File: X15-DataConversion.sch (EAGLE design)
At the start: 25 parts, among them Y1 ECS-80-18-4X

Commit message: layout mostly done
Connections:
- net 3.3V renamed 3V3
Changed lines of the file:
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@@
 <part name="R6" library="SparkFun-Resistors" deviceset="RESISTOR" device="0603" value="120"/>
 <part name="R7" library="SparkFun-Resistors" deviceset="RESISTOR" device="0603" value="120"/>
-<part name="GND10" library="supply1" library_urn="urn:adsk.eagle:library:371" deviceset="GND" device=""/>
 <part name="R9" library="SparkFun-Resistors" deviceset="RESISTOR" device="0603" value="0"/>
 <part name="C7" library="SparkFun-RF" deviceset="0.1UF" device="-0603-25V-5%" value="18pF"/>
@@
 <part name="R8" library="SparkFun-Resistors" deviceset="RESISTOR" device="0603" value="0"/>
 <part name="GND9" library="supply1" library_urn="urn:adsk.eagle:library:371" deviceset="GND" device=""/>
+<part name="GND10" library="supply1" library_urn="urn:adsk.eagle:library:371" deviceset="GND" device=""/>
 </parts>
 <sheets>
@@
 <attribute name="VALUE" x="111.76" y="46.736" size="1.778" layer="96" font="vector" align="top-center"/>
 </instance>
-<instance part="GND10" gate="1" x="101.6" y="66.04" smashed="yes" rot="R90">
-<attribute name="VALUE" x="104.14" y="63.5" size="1.778" layer="96" rot="R90"/>
-</instance>
 <instance part="R9" gate="G$1" x="147.32" y="40.64" smashed="yes" rot="R90">
 <attribute name="NAME" x="145.796" y="40.64" size="1.778" layer="95" font="vector" rot="R90" align="bottom-center"/>
@@
 <instance part="GND9" gate="1" x="99.06" y="40.64" smashed="yes">
 <attribute name="VALUE" x="96.52" y="38.1" size="1.778" layer="96"/>
+</instance>
+<instance part="GND10" gate="1" x="101.6" y="66.04" smashed="yes" rot="R90">
+<attribute name="VALUE" x="104.14" y="63.5" size="1.778" layer="96" rot="R90"/>
 </instance>
 </instances>
@@
 <wire x1="93.98" y1="165.1" x2="88.9" y2="165.1" width="0.1524" layer="91"/>
 <junction x="88.9" y="165.1"/>
-</segment>
-<segment>
-<pinref part="GND3" gate="1" pin="GND"/>
-<pinref part="STM" gate="G$1" pin="VSS_2"/>
-<wire x1="127" y1="93.98" x2="127" y2="99.06" width="0.1524" layer="91"/>
 </segment>
 <segment>
@@
 </segment>
 <segment>
-<pinref part="CAN_TRANCEIVER" gate="G$1" pin="RS"/>
-<pinref part="GND10" gate="1" pin="GND"/>
-<wire x1="93.98" y1="66.04" x2="99.06" y2="66.04" width="0.1524" layer="91"/>
-</segment>
-<segment>
 <pinref part="C7" gate="G$1" pin="2"/>
 <wire x1="137.16" y1="20.32" x2="137.16" y2="17.78" width="0.1524" layer="91"/>
@@
 <wire x1="99.06" y1="50.8" x2="99.06" y2="43.18" width="0.1524" layer="91"/>
 <pinref part="GND9" gate="1" pin="GND"/>
+</segment>
+<segment>
+<pinref part="GND3" gate="1" pin="GND"/>
+<pinref part="STM" gate="G$1" pin="VSS_2"/>
+<wire x1="127" y1="93.98" x2="127" y2="99.06" width="0.1524" layer="91"/>
+</segment>
+<segment>
+<pinref part="GND10" gate="1" pin="GND"/>
+<pinref part="CAN_TRANCEIVER" gate="G$1" pin="RS"/>
+<wire x1="99.06" y1="66.04" x2="93.98" y2="66.04" width="0.1524" layer="91"/>
 </segment>
 </net>
@@
 </segment>
 </net>
-<net name="3.3V" class="0">
+<net name="3V3" class="0">
 <segment>
 <pinref part="STM" gate="G$1" pin="VDDA"/>
@@
 <pinref part="STM" gate="G$1" pin="PF0-OSC_IN"/>
 <wire x1="78.74" y1="139.7" x2="68.58" y2="139.7" width="0.1524" layer="91"/>
+<label x="58.42" y="139.7" size="1.778" layer="95"/>
 </segment>
 <segment>
@@
 <pinref part="STM" gate="G$1" pin="PF1-OSC_OUT"/>
 <wire x1="78.74" y1="134.62" x2="68.58" y2="134.62" width="0.1524" layer="91"/>
-</segment>
-<segment>
+<label x="53.34" y="134.62" size="1.778" layer="95"/>
+</segment>
+<segment>

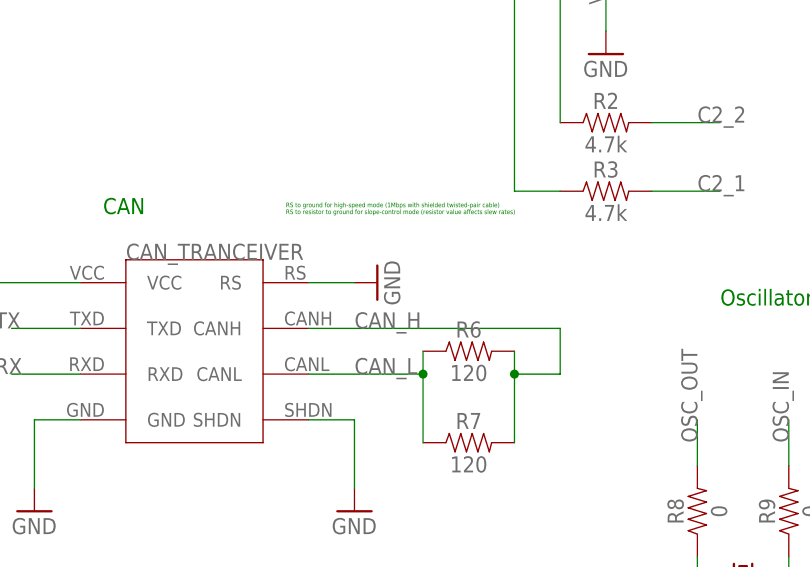
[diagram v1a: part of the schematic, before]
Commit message: fixing board layout
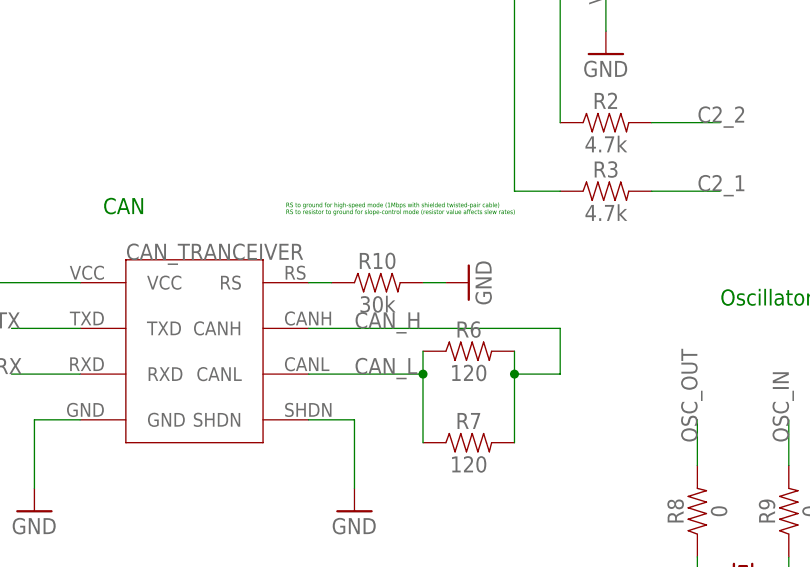
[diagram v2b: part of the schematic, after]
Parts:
- added R10: 30k, SparkFun-Resistors:RESISTOR0603
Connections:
- new net N$2: CAN_TRANCEIVER.RS, R10.1
- net GND: now also R10.2; no longer CAN_TRANCEIVER.RS
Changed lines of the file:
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@@
 <part name="GND9" library="supply1" library_urn="urn:adsk.eagle:library:371" deviceset="GND" device=""/>
 <part name="GND10" library="supply1" library_urn="urn:adsk.eagle:library:371" deviceset="GND" device=""/>
+<part name="R10" library="SparkFun-Resistors" deviceset="RESISTOR" device="0603" value="30k"/>
 </parts>
 <sheets>
@@
 <attribute name="VALUE" x="96.52" y="38.1" size="1.778" layer="96"/>
 </instance>
-<instance part="GND10" gate="1" x="101.6" y="66.04" smashed="yes" rot="R90">
-<attribute name="VALUE" x="104.14" y="63.5" size="1.778" layer="96" rot="R90"/>
+<instance part="GND10" gate="1" x="111.76" y="66.04" smashed="yes" rot="R90">
+<attribute name="VALUE" x="114.3" y="63.5" size="1.778" layer="96" rot="R90"/>
+</instance>
+<instance part="R10" gate="G$1" x="101.6" y="66.04" smashed="yes">
+<attribute name="NAME" x="101.6" y="67.564" size="1.778" layer="95" font="vector" align="bottom-center"/>
+<attribute name="VALUE" x="101.6" y="64.516" size="1.778" layer="96" font="vector" align="top-center"/>
 </instance>
 </instances>
@@
 </segment>
 <segment>
+<pinref part="R10" gate="G$1" pin="2"/>
 <pinref part="GND10" gate="1" pin="GND"/>
-<pinref part="CAN_TRANCEIVER" gate="G$1" pin="RS"/>
-<wire x1="99.06" y1="66.04" x2="93.98" y2="66.04" width="0.1524" layer="91"/>
+<wire x1="106.68" y1="66.04" x2="109.22" y2="66.04" width="0.1524" layer="91"/>
 </segment>
 </net>
@@
 </segment>
 </net>
+<net name="N$2" class="0">
+<segment>
+<pinref part="CAN_TRANCEIVER" gate="G$1" pin="RS"/>
+<pinref part="R10" gate="G$1" pin="1"/>
+<wire x1="93.98" y1="66.04" x2="96.52" y2="66.04" width="0.1524" layer="91"/>
+</segment>
+</net>

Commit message: cleaning up board layout
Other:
- note removed: "RS to ground for high-speed mode (1Mbps with shielded twisted-pair cable) RS to resistor to ground for slope-control mode (resistor value affects slew rates)"
- moved on the sheet: C6, CAN_TRANCEIVER, CONNECTOR1, D3, R10, R5, R6, R7, U$1

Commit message: alumni review changes
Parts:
- removed D1: Green, SparkFun-LED:LED-GREEN-0603-WE
- removed D3: Orange, SparkFun-LED:LED0603
- added LED1, LED2: LSM0805452VLED_05452V_VCC, X15-Data-Conversion-Parts:LSM0805452VLED_05452V_VCC
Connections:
- net GND: now also LED1.2, LED2.2; no longer D1.C, D3.C
- net N$1: now also LED1.1; no longer D3.A
- net N$11: now also LED2.1; no longer D1.A
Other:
- moved on the sheet: R6, R7

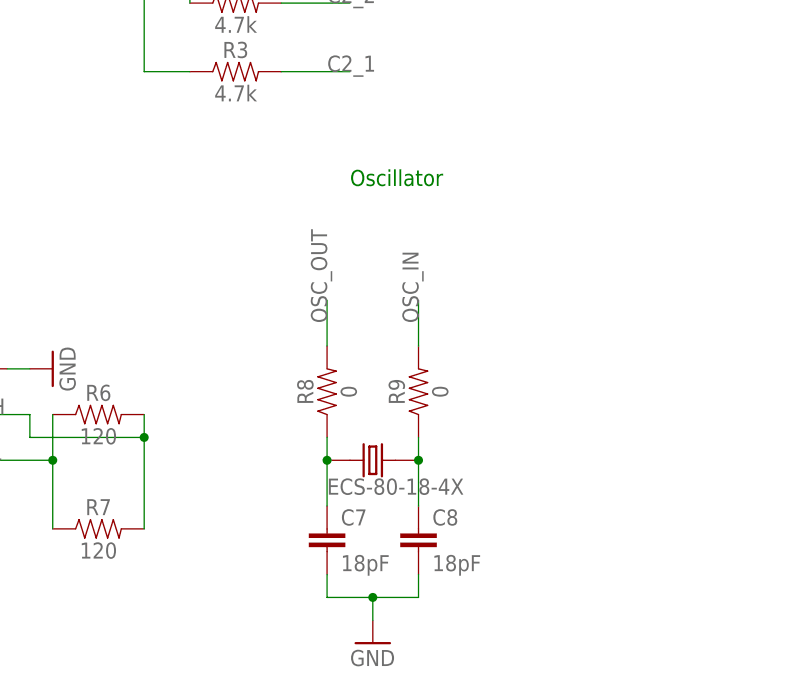
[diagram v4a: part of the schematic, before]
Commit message: removed oscillator and fixed trace widths
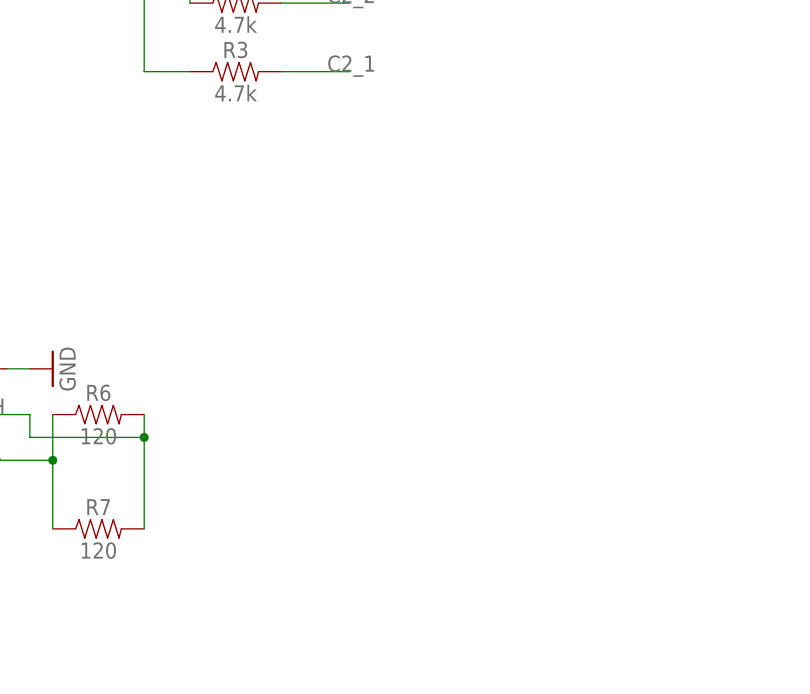
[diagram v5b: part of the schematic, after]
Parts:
- removed C7, C8: 18pF, SparkFun-RF:0.1UF-0603-25V-5%
- removed R8, R9: 0, SparkFun-Resistors:RESISTOR0603
- removed Y1: ECS-80-18-4X, X15-Data-Conversion-Parts:ECS-80-18-4X
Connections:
- removed net N$3: C7.1, R8.1, Y1.1
- removed net N$4: C8.1, R9.1, Y1.2
- net GND: no longer C7.2, C8.2
- net OSC_IN: no longer R9.2
- net OSC_OUT: no longer R8.2
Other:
- note removed: "Oscillator"
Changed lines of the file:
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@@
 <part name="GND7" library="supply1" library_urn="urn:adsk.eagle:library:371" deviceset="GND" device=""/>
 <part name="GND8" library="supply1" library_urn="urn:adsk.eagle:library:371" deviceset="GND" device=""/>
-<part name="R9" library="SparkFun-Resistors" deviceset="RESISTOR" device="0603" value="0"/>
-<part name="C7" library="SparkFun-RF" deviceset="0.1UF" device="-0603-25V-5%" value="18pF"/>
-<part name="C8" library="SparkFun-RF" deviceset="0.1UF" device="-0603-25V-5%" value="18pF"/>
-<part name="GND11" library="supply1" library_urn="urn:adsk.eagle:library:371" deviceset="GND" device=""/>
-<part name="Y1" library="X15-Data-Conversion-Parts" deviceset="ECS-80-18-4X" device="" package3d_urn="urn:adsk.eagle:package:38192067/2"/>
-<part name="R8" library="SparkFun-Resistors" deviceset="RESISTOR" device="0603" value="0"/>
 <part name="GND9" library="supply1" library_urn="urn:adsk.eagle:library:371" deviceset="GND" device=""/>
 <part name="GND10" library="supply1" library_urn="urn:adsk.eagle:library:371" deviceset="GND" device=""/>
@@
 <text x="205.74" y="81.28" size="1.778" layer="91">Connectors</text>
 <text x="66.04" y="50.8" size="1.778" layer="91">CAN</text>
-<text x="139.7" y="63.5" size="1.778" layer="91">Oscillator</text>
 <text x="190.5" y="152.4" size="1.778" layer="91">Pin 1 (VDD)</text>
 <text x="210.82" y="152.4" size="1.778" layer="91">Pin 17 (VDDIO2)</text>
@@
 <instance part="GND8" gate="1" x="58.42" y="17.78" smashed="yes">
 <attribute name="VALUE" x="55.88" y="15.24" size="1.778" layer="96"/>
-</instance>
-<instance part="R9" gate="G$1" x="147.32" y="40.64" smashed="yes" rot="R90">
-<attribute name="NAME" x="145.796" y="40.64" size="1.778" layer="95" font="vector" rot="R90" align="bottom-center"/>
-<attribute name="VALUE" x="148.844" y="40.64" size="1.778" layer="96" font="vector" rot="R90" align="top-center"/>
-</instance>
-<instance part="C7" gate="G$1" x="137.16" y="22.86" smashed="yes">
-<attribute name="NAME" x="138.684" y="25.781" size="1.778" layer="95" font="vector"/>
-<attribute name="VALUE" x="138.684" y="20.701" size="1.778" layer="96" font="vector"/>
-</instance>
-<instance part="C8" gate="G$1" x="147.32" y="22.86" smashed="yes">
-<attribute name="NAME" x="148.844" y="25.781" size="1.778" layer="95" font="vector"/>
-<attribute name="VALUE" x="148.844" y="20.701" size="1.778" layer="96" font="vector"/>
-</instance>
-<instance part="GND11" gate="1" x="142.24" y="12.7" smashed="yes">
-<attribute name="VALUE" x="139.7" y="10.16" size="1.778" layer="96"/>
-</instance>
-<instance part="Y1" gate="G$1" x="142.24" y="33.02" smashed="yes">
-<attribute name="VALUE" x="137.14506875" y="29.19645" size="1.78431875" layer="96"/>
-</instance>
-<instance part="R8" gate="G$1" x="137.16" y="40.64" smashed="yes" rot="R90">
-<attribute name="NAME" x="135.636" y="40.64" size="1.778" layer="95" font="vector" rot="R90" align="bottom-center"/>
-<attribute name="VALUE" x="138.684" y="40.64" size="1.778" layer="96" font="vector" rot="R90" align="top-center"/>
 </instance>
 <instance part="GND9" gate="1" x="93.98" y="17.78" smashed="yes">
@@
 </segment>
 <segment>
-<pinref part="C7" gate="G$1" pin="2"/>
-<wire x1="137.16" y1="20.32" x2="137.16" y2="17.78" width="0.1524" layer="91"/>
-<wire x1="137.16" y1="17.78" x2="142.24" y2="17.78" width="0.1524" layer="91"/>
-<pinref part="C8" gate="G$1" pin="2"/>
-<wire x1="142.24" y1="17.78" x2="147.32" y2="17.78" width="0.1524" layer="91"/>
-<wire x1="147.32" y1="17.78" x2="147.32" y2="20.32" width="0.1524" layer="91"/>
-<wire x1="142.24" y1="17.78" x2="142.24" y2="15.24" width="0.1524" layer="91"/>
-<junction x="142.24" y="17.78"/>
-<pinref part="GND11" gate="1" pin="GND"/>
-</segment>
-<segment>
 <pinref part="CAN_TRANCEIVER" gate="G$1" pin="SHDN"/>
 <wire x1="88.9" y1="27.94" x2="93.98" y2="27.94" width="0.1524" layer="91"/>
@@
 <label x="58.42" y="139.7" size="1.778" layer="95"/>
 </segment>
-<segment>
-<pinref part="R9" gate="G$1" pin="2"/>
-<wire x1="147.32" y1="45.72" x2="147.32" y2="50.8" width="0.1524" layer="91"/>
-<label x="147.32" y="48.26" size="1.778" layer="95" rot="R90"/>
-</segment>
 </net>
 <net name="OSC_OUT" class="0">
@@
 <label x="53.34" y="134.62" size="1.778" layer="95"/>
 </segment>
-<segment>
-<pinref part="R8" gate="G$1" pin="2"/>
-<wire x1="137.16" y1="45.72" x2="137.16" y2="50.8" width="0.1524" layer="91"/>
-<label x="137.16" y="48.26" size="1.778" layer="95" rot="R90"/>
-</segment>
-</net>
-<net name="N$3" class="0">
-<segment>
-<pinref part="Y1" gate="G$1" pin="1"/>
-<pinref part="R8" gate="G$1" pin="1"/>
-<wire x1="137.16" y1="33.02" x2="137.16" y2="35.56" width="0.1524" layer="91"/>
-<pinref part="C7" gate="G$1" pin="1"/>
-<wire x1="137.16" y1="27.94" x2="137.16" y2="33.02" width="0.1524" layer="91"/>
-<junction x="137.16" y="33.02"/>
-</segment>
-</net>
-<net name="N$4" class="0">
-<segment>
-<pinref part="Y1" gate="G$1" pin="2"/>
-<pinref part="R9" gate="G$1" pin="1"/>
-<wire x1="147.32" y1="33.02" x2="147.32" y2="35.56" width="0.1524" layer="91"/>
-<pinref part="C8" gate="G$1" pin="1"/>
-<wire x1="147.32" y1="27.94" x2="147.32" y2="33.02" width="0.1524" layer="91"/>
-<junction x="147.32" y="33.02"/>
-</segment>
-</net>
+</net>

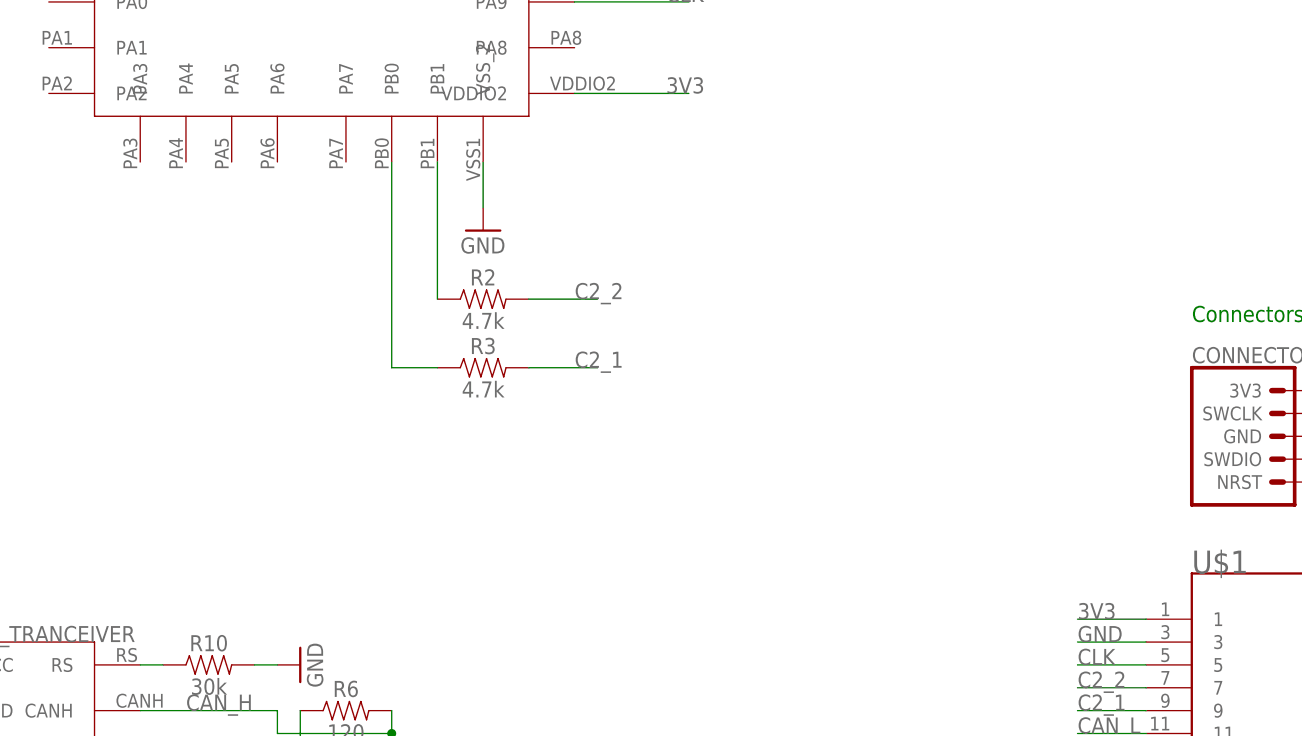
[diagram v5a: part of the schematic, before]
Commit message: added 5 pin connector
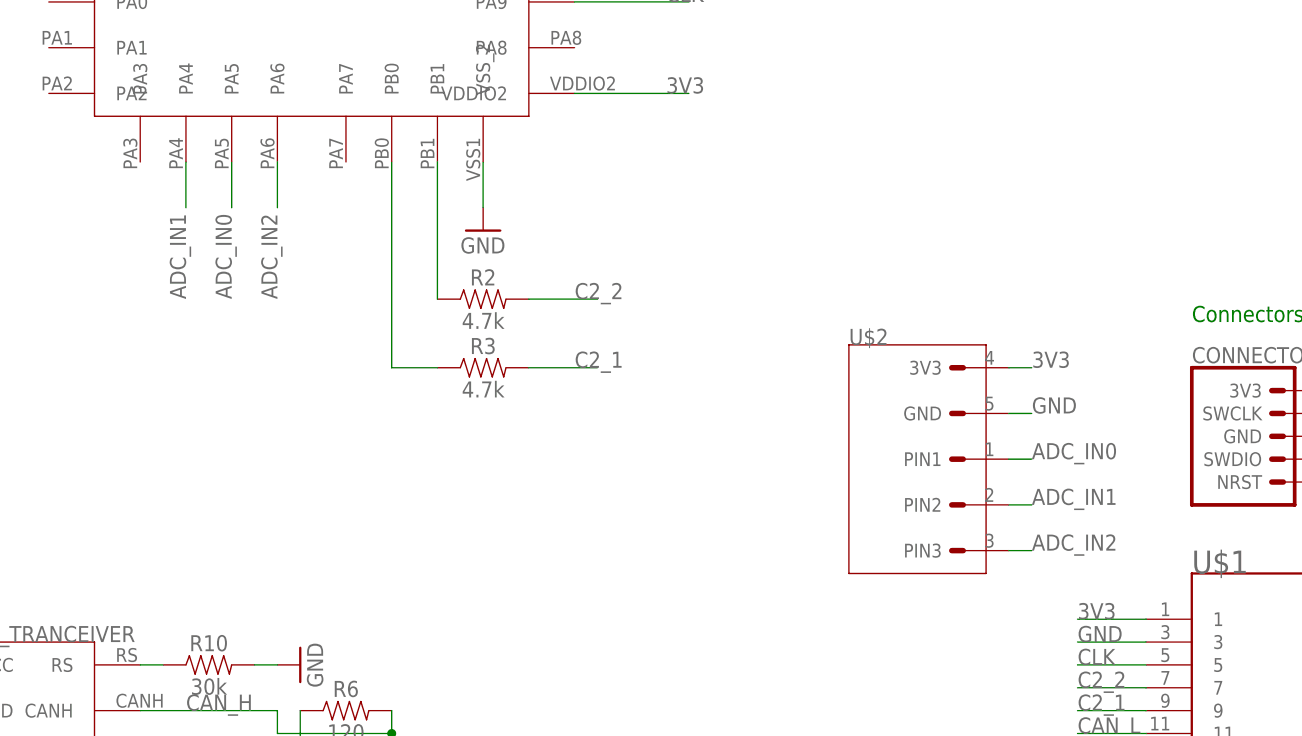
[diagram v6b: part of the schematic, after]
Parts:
- added U$2: STM_CONN, X15-Data-Conversion-Parts:STM_CONN
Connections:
- new net ADC_IN0: STM.PA5, U$2.PIN1
- new net ADC_IN1: STM.PA4, U$2.PIN2
- new net ADC_IN2: STM.PA6, U$2.PIN3
- net 3V3: now also U$2.3V3
- net GND: now also U$2.GND
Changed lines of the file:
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@@
 <part name="R6" library="SparkFun-Resistors" deviceset="RESISTOR" device="0603" value="120"/>
 <part name="R7" library="SparkFun-Resistors" deviceset="RESISTOR" device="0603" value="120"/>
+<part name="U$2" library="X15-Data-Conversion-Parts" deviceset="STM_CONN" device="" package3d_urn="urn:adsk.eagle:package:38192072/1"/>
 </parts>
 <sheets>
@@
 <attribute name="VALUE" x="111.76" y="23.876" size="1.778" layer="96" font="vector" align="top-center"/>
 </instance>
+<instance part="U$2" gate="G$1" x="175.26" y="68.58" smashed="yes">
+<attribute name="NAME" x="167.64" y="78.74" size="1.778" layer="95"/>
+</instance>
 </instances>
 <busses>
@@
 <wire x1="144.78" y1="154.94" x2="144.78" y2="157.48" width="0.1524" layer="91"/>
 </segment>
+<segment>
+<pinref part="U$2" gate="G$1" pin="GND"/>
+<wire x1="185.42" y1="71.12" x2="187.96" y2="71.12" width="0.1524" layer="91"/>
+<label x="187.96" y="71.12" size="1.778" layer="95"/>
+</segment>
 </net>
 <net name="NRST" class="0">
@@
 <label x="20.32" y="147.32" size="1.778" layer="95" rot="R90"/>
 </segment>
+<segment>
+<pinref part="U$2" gate="G$1" pin="3V3"/>
+<wire x1="185.42" y1="76.2" x2="187.96" y2="76.2" width="0.1524" layer="91"/>
+<label x="187.96" y="76.2" size="1.778" layer="95"/>
+</segment>
 </net>
 <net name="ALERT1" class="0">
@@
 </segment>
 </net>
+<net name="ADC_IN0" class="0">
+<segment>
+<pinref part="U$2" gate="G$1" pin="PIN1"/>
+<wire x1="185.42" y1="66.04" x2="187.96" y2="66.04" width="0.1524" layer="91"/>
+<label x="187.96" y="66.04" size="1.778" layer="95"/>
+</segment>
+<segment>
+<pinref part="STM" gate="G$1" pin="PA5"/>
+<wire x1="99.06" y1="99.06" x2="99.06" y2="93.98" width="0.1524" layer="91"/>
+<label x="99.06" y="83.82" size="1.778" layer="95" rot="R90"/>
+</segment>
+</net>
+<net name="ADC_IN1" class="0">
+<segment>
+<pinref part="U$2" gate="G$1" pin="PIN2"/>
+<wire x1="185.42" y1="60.96" x2="187.96" y2="60.96" width="0.1524" layer="91"/>
+<label x="187.96" y="60.96" size="1.778" layer="95"/>
+</segment>
+<segment>
+<pinref part="STM" gate="G$1" pin="PA4"/>
+<wire x1="93.98" y1="99.06" x2="93.98" y2="93.98" width="0.1524" layer="91"/>
+<label x="93.98" y="83.82" size="1.778" layer="95" rot="R90"/>
+</segment>
+</net>
+<net name="ADC_IN2" class="0">
+<segment>
+<pinref part="STM" gate="G$1" pin="PA6"/>
+<wire x1="104.14" y1="99.06" x2="104.14" y2="93.98" width="0.1524" layer="91"/>
+<label x="104.14" y="83.82" size="1.778" layer="95" rot="R90"/>
+</segment>
+<segment>
+<pinref part="U$2" gate="G$1" pin="PIN3"/>
+<wire x1="185.42" y1="55.88" x2="187.96" y2="55.88" width="0.1524" layer="91"/>
+<label x="187.96" y="55.88" size="1.778" layer="95"/>
+</segment>
+</net>
